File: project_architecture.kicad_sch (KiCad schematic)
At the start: 0 parts

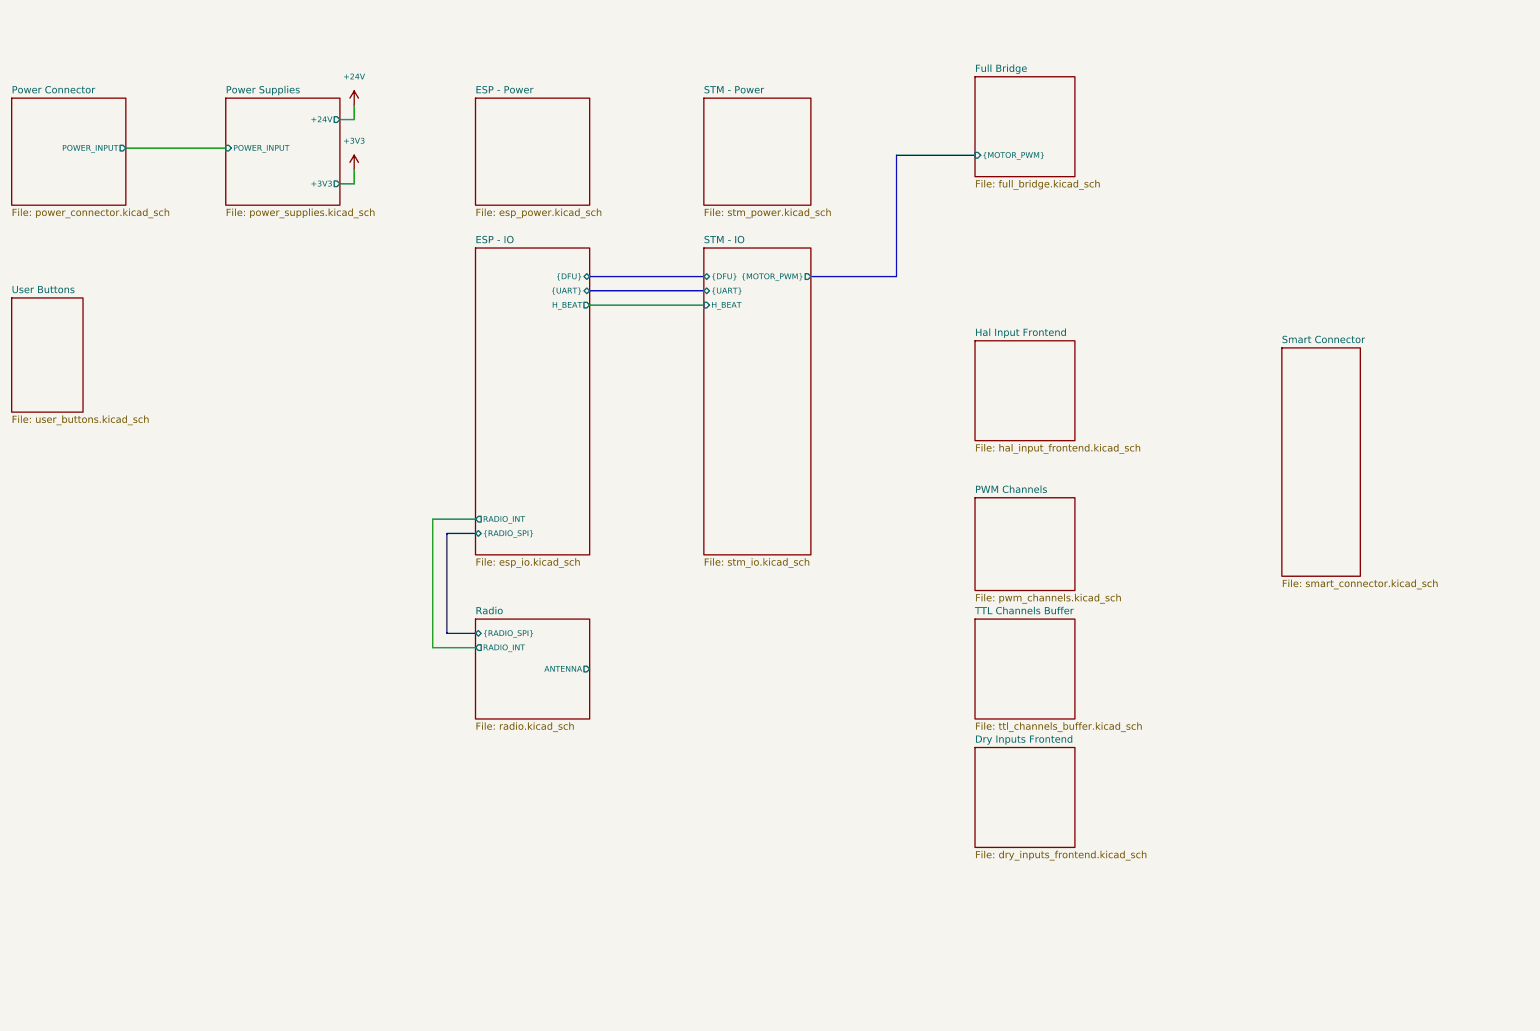
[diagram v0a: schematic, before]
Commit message: schematic: continue project architecture
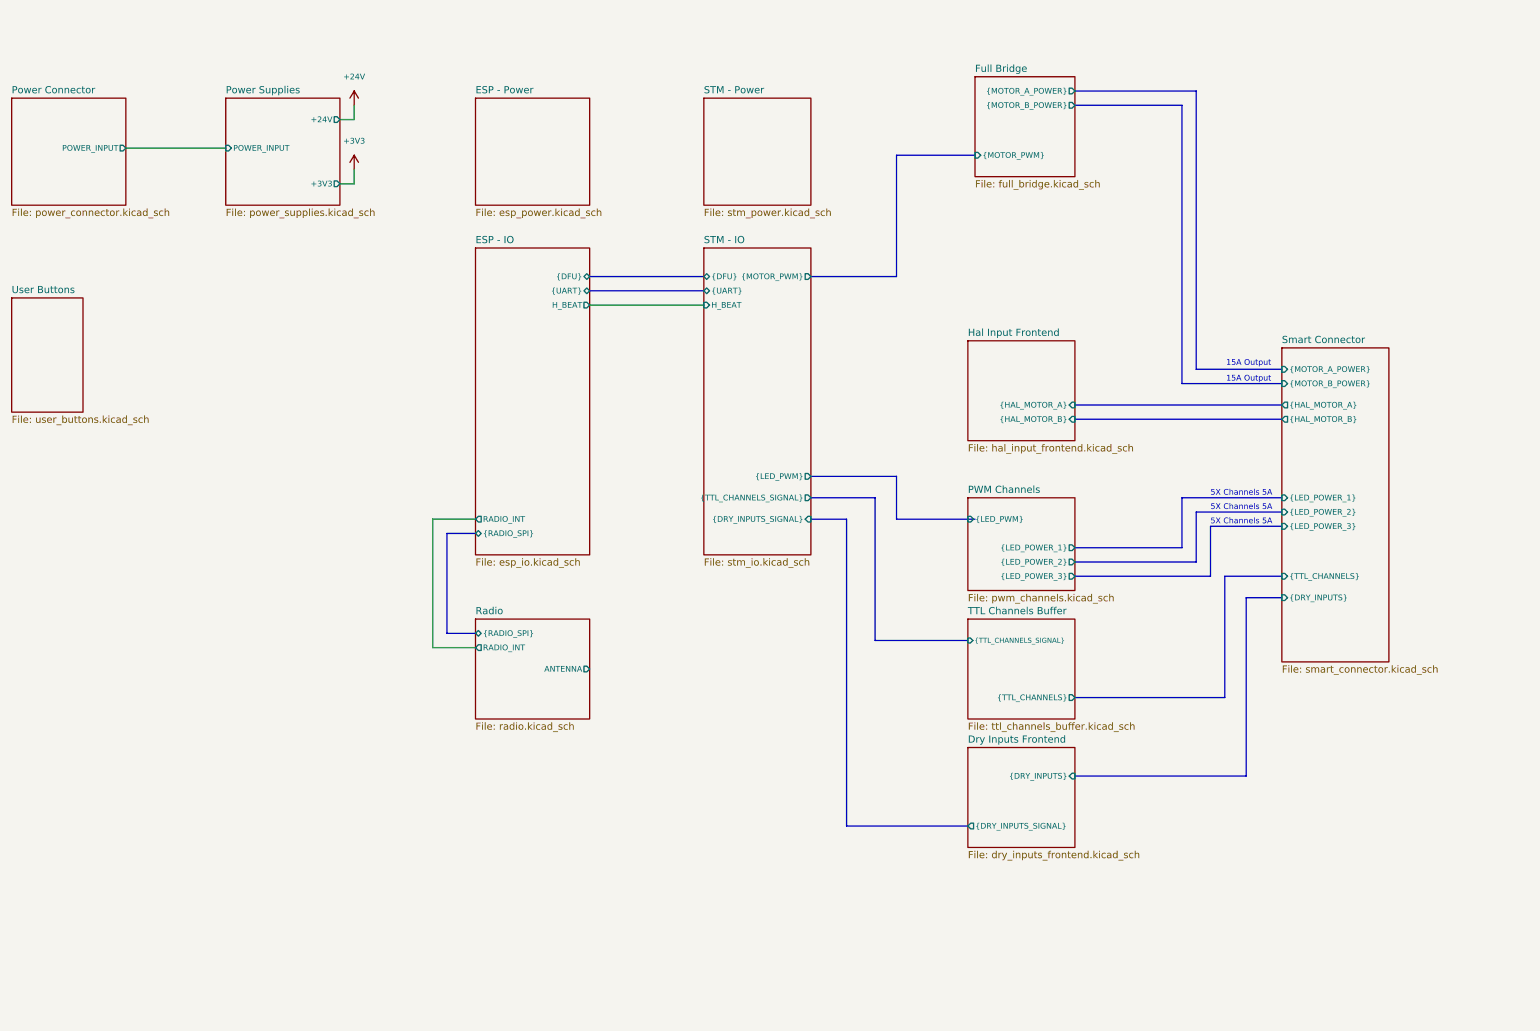
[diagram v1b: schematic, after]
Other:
- sheet Dry Inputs Frontend ports: added {DRY_INPUTS_SIGNAL}, {DRY_INPUTS}; removed none
- sheet Full Bridge ports: added {MOTOR_A_POWER}, {MOTOR_B_POWER}; removed none
- sheet Hal Input Frontend ports: added {HAL_MOTOR_A}, {HAL_MOTOR_B}; removed none
- sheet PWM Channels ports: added {LED_POWER_1}, {LED_POWER_2}, {LED_POWER_3}, {LED_PWM}; removed none
- sheet STM - IO ports: added {DRY_INPUTS_SIGNAL}, {LED_PWM}, {TTL_CHANNELS_SIGNAL}; removed none
- sheet Smart Connector ports: added {DRY_INPUTS}, {HAL_MOTOR_A}, {HAL_MOTOR_B}, {LED_POWER_1}, {LED_POWER_2}, {LED_POWER_3}, {MOTOR_A_POWER}, {MOTOR_B_POWER}, {TTL_CHANNELS}; removed none
- sheet TTL Channels Buffer ports: added {TTL_CHANNELS_SIGNAL}, {TTL_CHANNELS}; removed none
- note added: "15A Output"
- note added: "5X Channels 5A"

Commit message: schematic: add project structure wiring
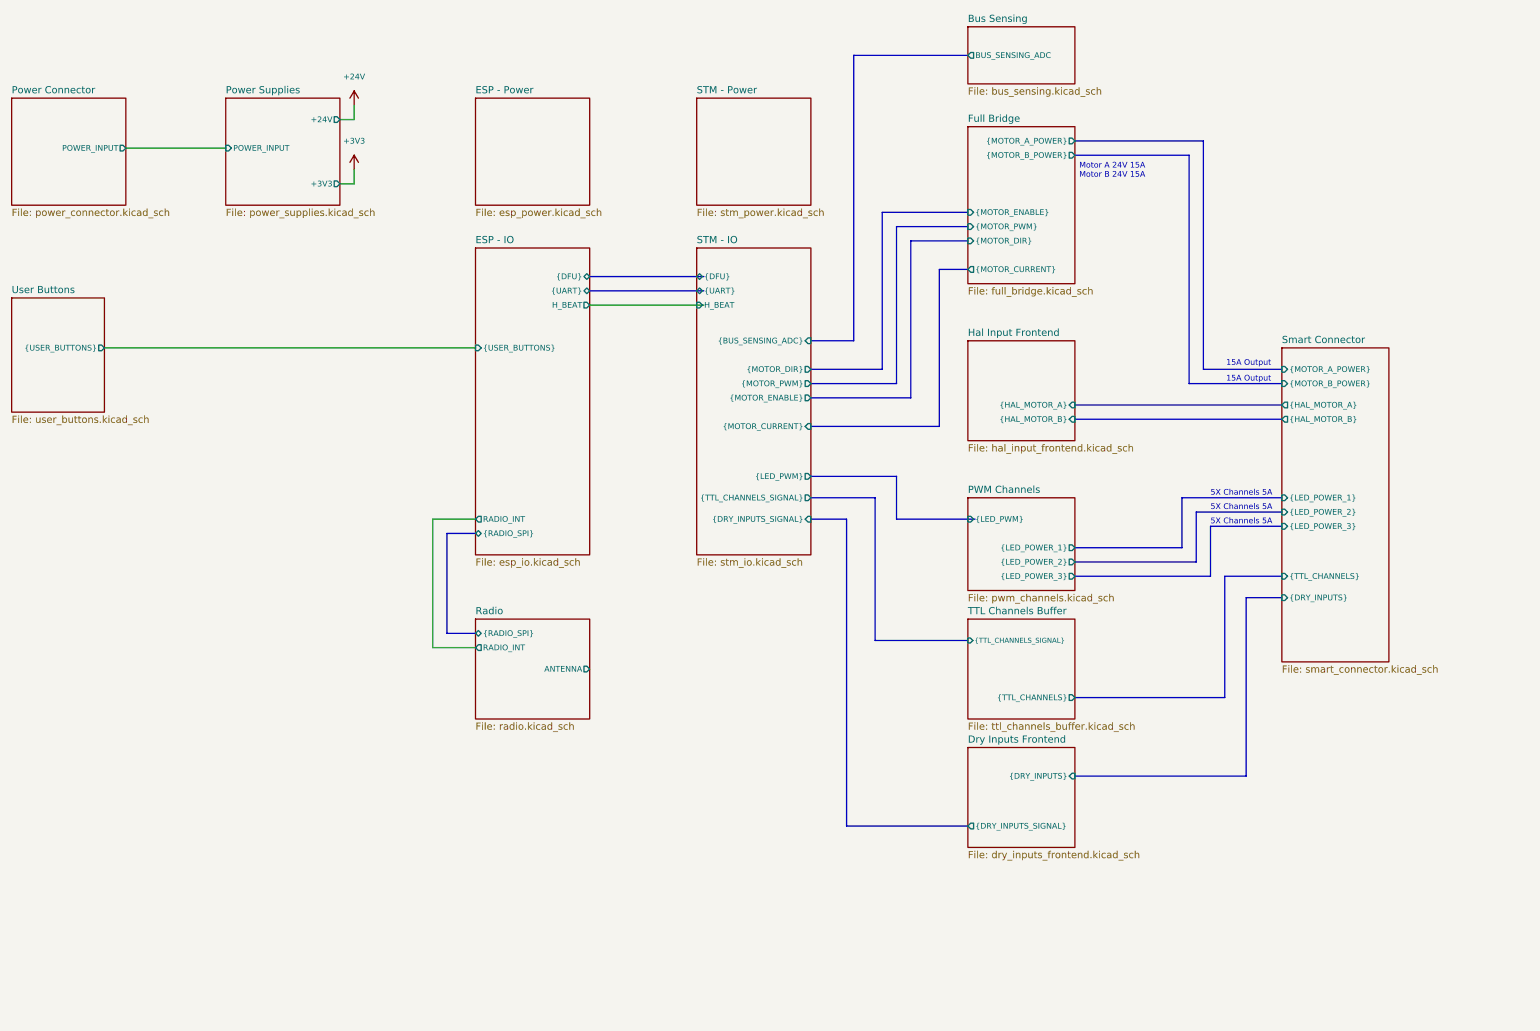
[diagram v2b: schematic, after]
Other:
- added sheet Bus Sensing (bus_sensing.kicad_sch)
- sheet ESP - IO ports: added {USER_BUTTONS}; removed none
- sheet Full Bridge ports: added {MOTOR_CURRENT}, {MOTOR_DIR}, {MOTOR_ENABLE}; removed none
- sheet STM - IO ports: added {BUS_SENSING_ADC}, {MOTOR_CURRENT}, {MOTOR_DIR}, {MOTOR_ENABLE}; removed none
- sheet User Buttons ports: added {USER_BUTTONS}; removed none
- note added: "Motor A 24V 15A Motor B 24V 15A"

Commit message: Add power stages
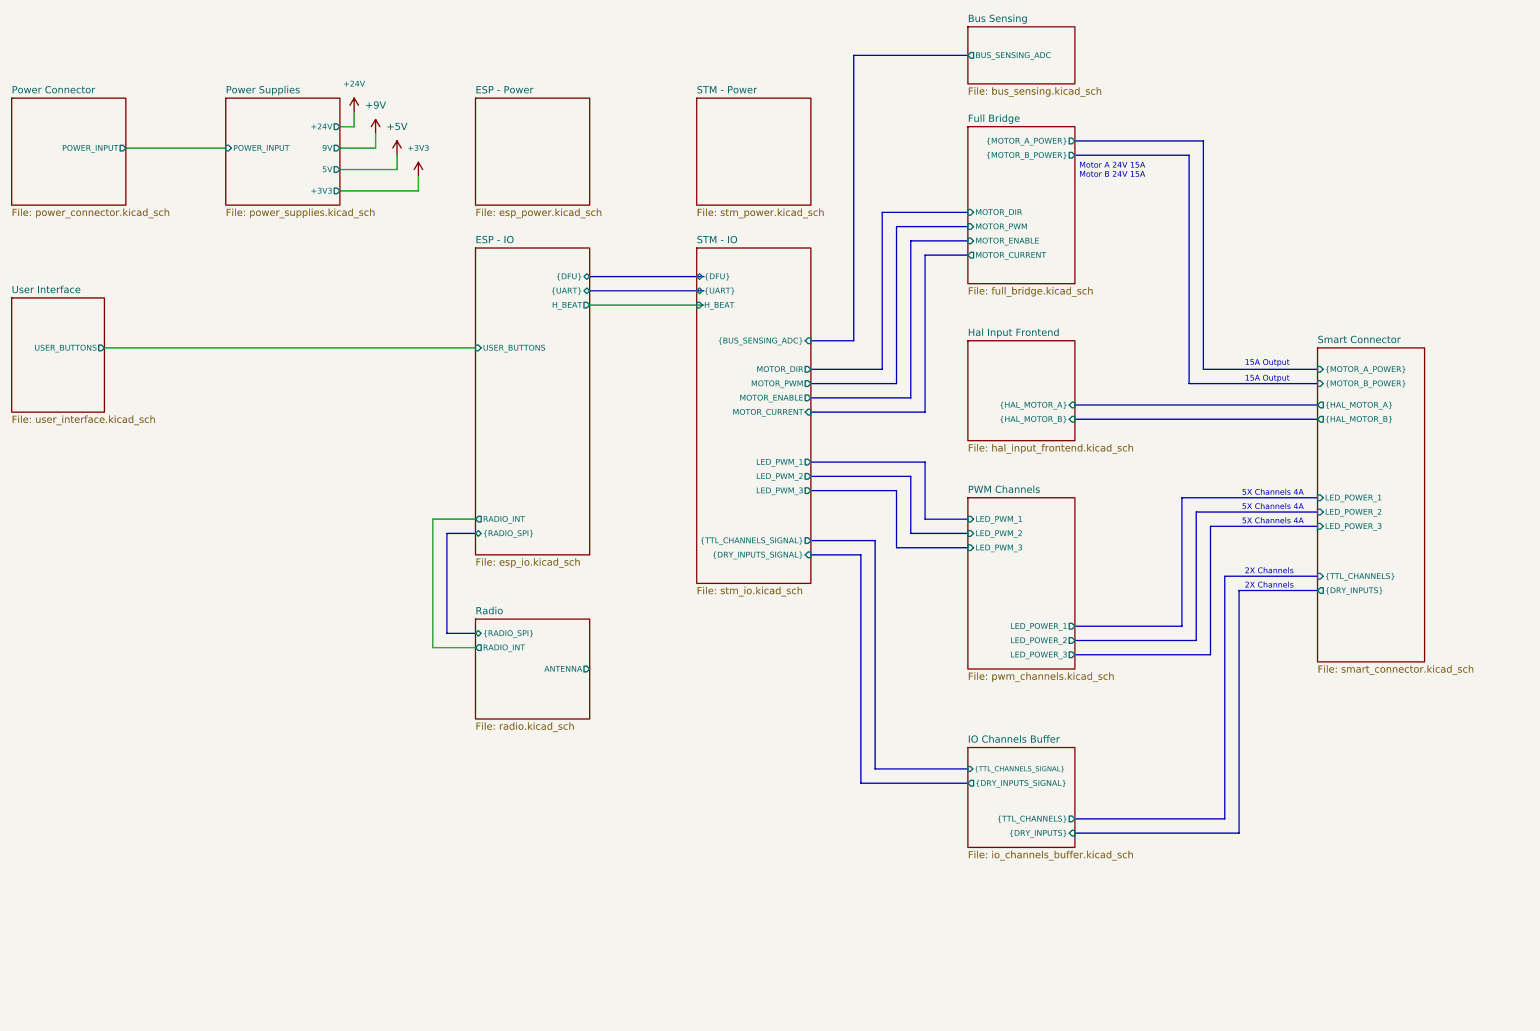
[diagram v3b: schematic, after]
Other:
- sheet TTL Channels Buffer renamed IO Channels Buffer
- sheet User Buttons renamed User Interface
- removed sheet Dry Inputs Frontend
- sheet ESP - IO ports: added USER_BUTTONS; removed {USER_BUTTONS}
- sheet Full Bridge ports: added MOTOR_CURRENT, MOTOR_DIR, MOTOR_ENABLE, MOTOR_PWM; removed {MOTOR_CURRENT}, {MOTOR_DIR}, {MOTOR_ENABLE}, {MOTOR_PWM}
- sheet IO Channels Buffer: file ttl_channels_buffer.kicad_sch -> io_channels_buffer.kicad_sch
- sheet IO Channels Buffer ports: added {DRY_INPUTS_SIGNAL}, {DRY_INPUTS}; removed none
- sheet PWM Channels ports: added LED_POWER_1, LED_POWER_2, LED_POWER_3, LED_PWM_1, LED_PWM_2, LED_PWM_3; removed {LED_POWER_1}, {LED_POWER_2}, {LED_POWER_3}, {LED_PWM}
- sheet Power Supplies ports: added 5V, 9V; removed none
- sheet STM - IO ports: added LED_PWM_1, LED_PWM_2, LED_PWM_3, MOTOR_CURRENT, MOTOR_DIR, MOTOR_ENABLE, MOTOR_PWM; removed {LED_PWM}, {MOTOR_CURRENT}, {MOTOR_DIR}, {MOTOR_ENABLE}, {MOTOR_PWM}
- sheet Smart Connector ports: added LED_POWER_1, LED_POWER_2, LED_POWER_3; removed {LED_POWER_1}, {LED_POWER_2}, {LED_POWER_3}
- sheet User Interface: file user_buttons.kicad_sch -> user_interface.kicad_sch
- sheet User Interface ports: added USER_BUTTONS; removed {USER_BUTTONS}
- note added: "2X Channels"
- note added: "5X Channels 4A"
- note removed: "5X Channels 5A"

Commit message: Add power supplies
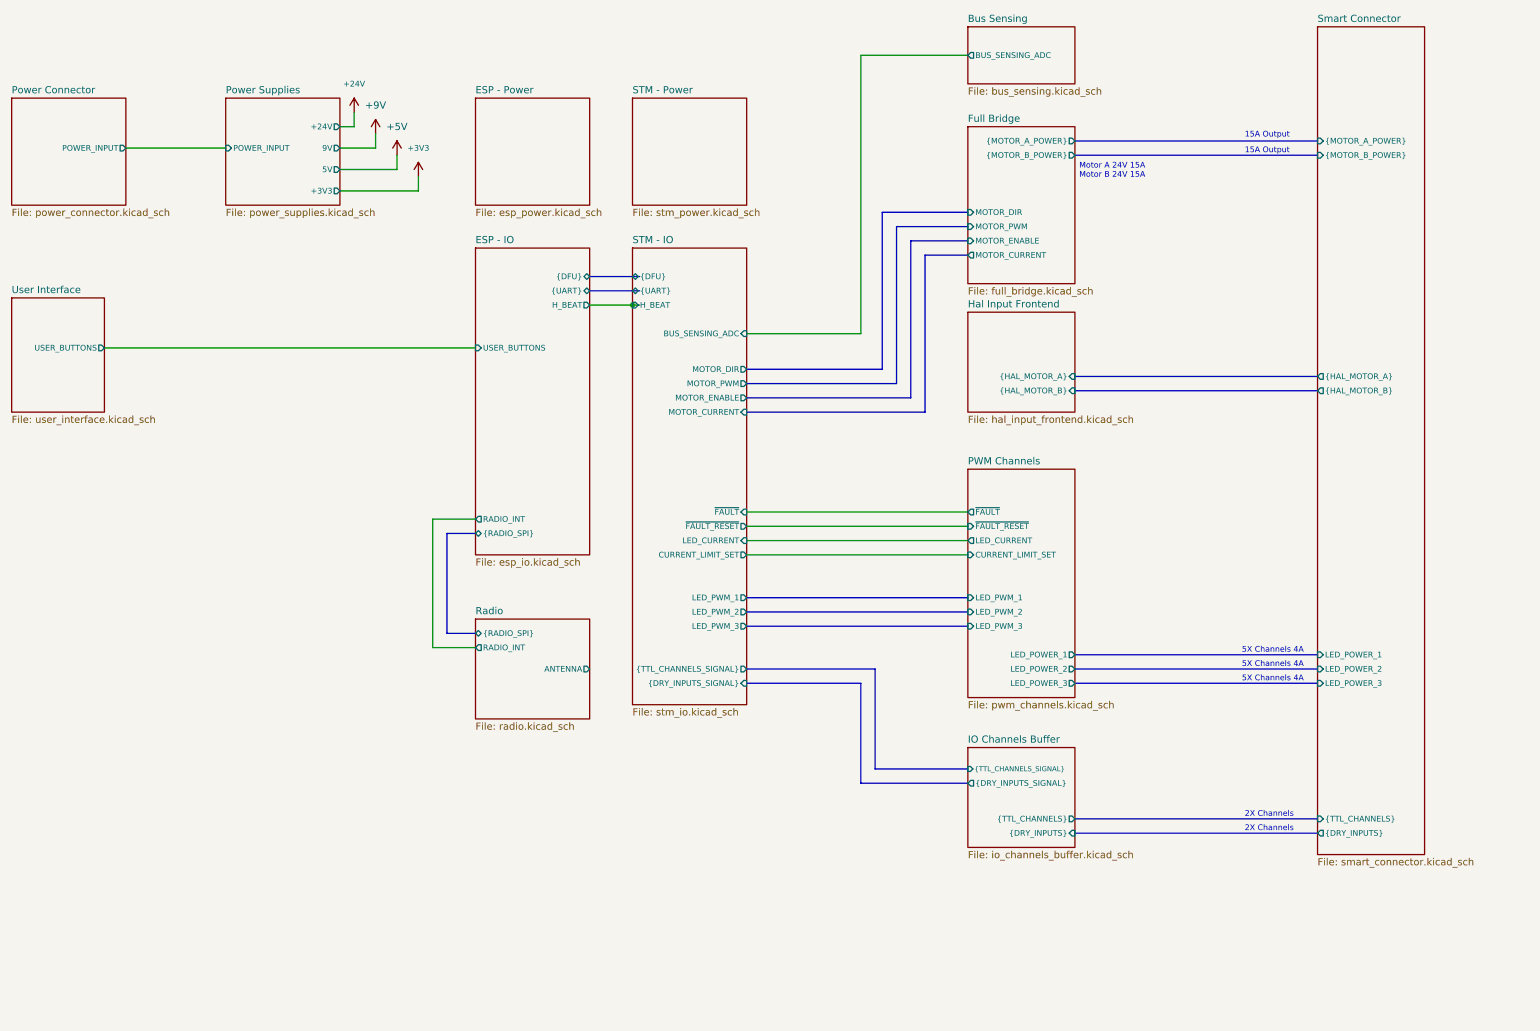
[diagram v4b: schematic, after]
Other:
- sheet PWM Channels ports: added CURRENT_LIMIT_SET, LED_CURRENT, ~{FAULT_RESET}, ~{FAULT}; removed none
- sheet STM - IO ports: added BUS_SENSING_ADC, CURRENT_LIMIT_SET, LED_CURRENT, ~{FAULT_RESET}, ~{FAULT}; removed {BUS_SENSING_ADC}

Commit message: Remove STM
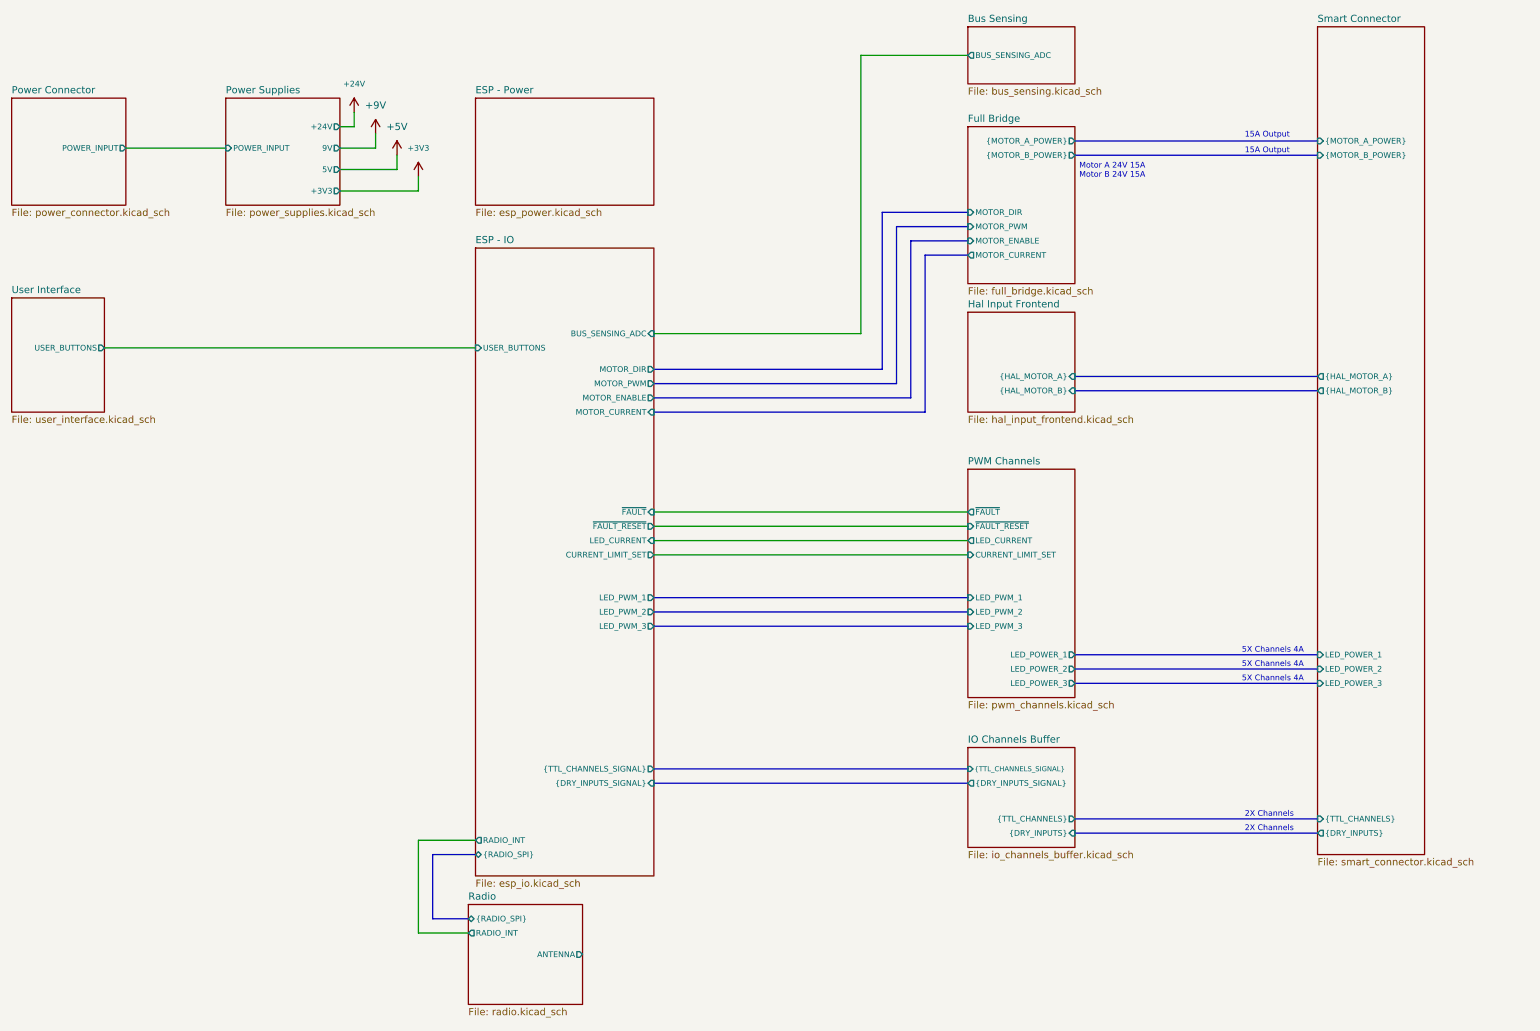
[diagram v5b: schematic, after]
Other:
- removed sheet STM - IO
- removed sheet STM - Power
- sheet ESP - IO ports: added BUS_SENSING_ADC, CURRENT_LIMIT_SET, LED_CURRENT, LED_PWM_1, LED_PWM_2, LED_PWM_3, MOTOR_CURRENT, MOTOR_DIR, MOTOR_ENABLE, MOTOR_PWM, {DRY_INPUTS_SIGNAL}, {TTL_CHANNELS_SIGNAL}, ~{FAULT_RESET}, ~{FAULT}; removed H_BEAT, {DFU}, {UART}
